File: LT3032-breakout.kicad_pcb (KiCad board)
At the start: 2 copper layers, 26 x 15.4 mm, 10 parts, among them J1 CONN_01X03, J2 CONN_01X03, U1 LT3032-X

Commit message: Added version number
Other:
- board text added: "LT3032 Breakout Board v2.0 https://github.com/PatrickBaus"
- board text removed: "LT3032 Breakout Board https://github.com/PatrickBaus"
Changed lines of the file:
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@@
     )
   )
-  (gr_text "LT3032 Breakout Board\nhttps://github.com/PatrickBaus" (at 163.6 77.6) (layer B.SilkS)
+  (gr_text "LT3032 Breakout Board v2.0\nhttps://github.com/PatrickBaus" (at 163.6 77.6) (layer B.SilkS)
     (effects (font (size 0.8 0.8) (thickness 0.15)) (justify left mirror))
   )

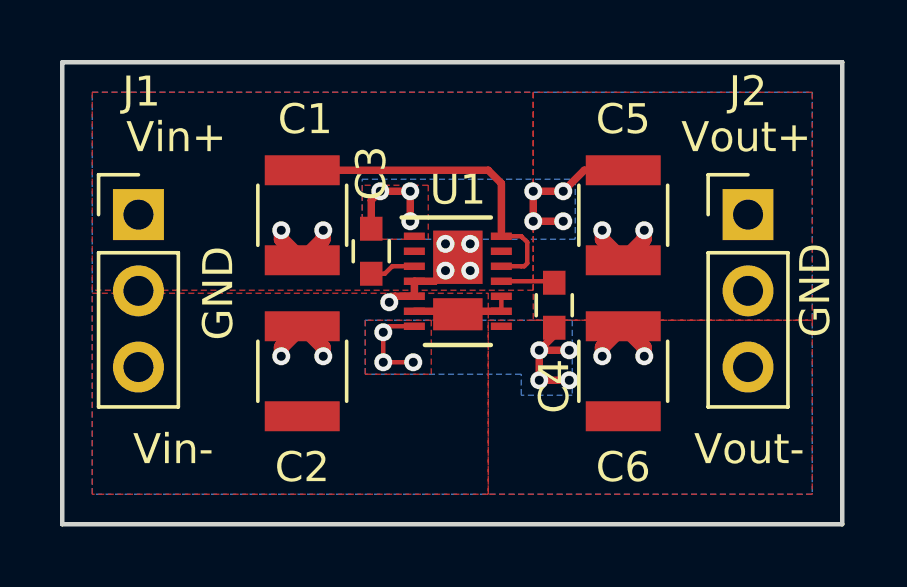
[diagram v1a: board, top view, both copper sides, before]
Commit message: Updated schematic to KiCAD v5.0
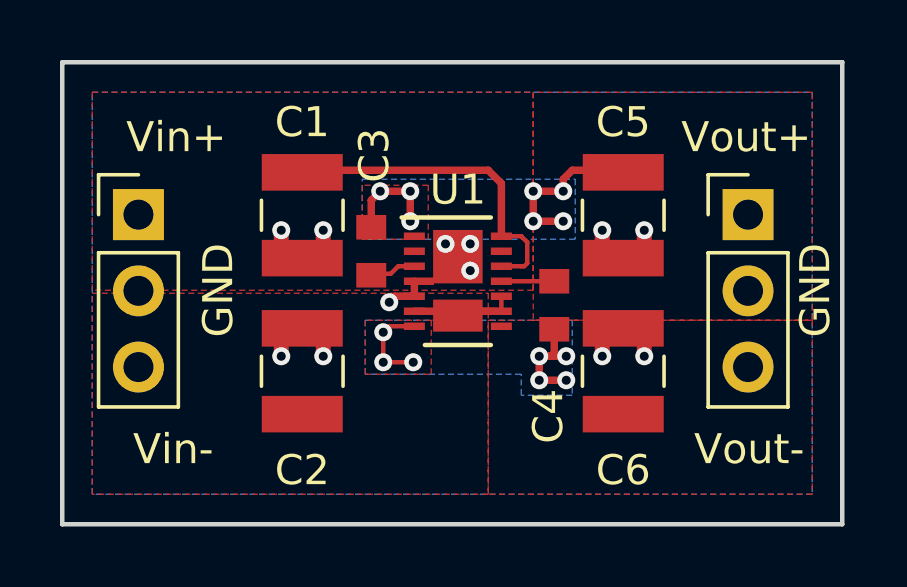
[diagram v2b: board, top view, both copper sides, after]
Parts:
- C1, C2, C5, C6: footprint Capacitors_SMD:C_1210 -> Capacitor_SMD:C_1210_3225Metric
- C3, C4: footprint Capacitors_SMD:C_0603 -> Capacitor_SMD:C_0603_1608Metric
- J1: value CONN_01X03 -> Input; footprint Pin_Headers:Pin_Header_Straight_1x03_Pitch2.54mm -> Connector_PinHeader_2.54mm:PinHeader_1x03_P2.54mm_Vertical
- J2: value CONN_01X03 -> Output; footprint Pin_Headers:Pin_Header_Straight_1x03_Pitch2.54mm -> Connector_PinHeader_2.54mm:PinHeader_1x03_P2.54mm_Vertical
- U1: footprint Custom_footprints:DFN-14-1EP_3x4mm_Pitch0.5mm_2Pads -> Package_DFN_QFN:Linear_DE14MA
- moved #LOGO1 0.10 mm to (153.9, 71.4)
- renumbered REF*** to #LOGO1
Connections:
- net INN renamed /INN
- net Net-(C1-Pad2) renamed /INP
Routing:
- net GND: vias 13 -> 12
